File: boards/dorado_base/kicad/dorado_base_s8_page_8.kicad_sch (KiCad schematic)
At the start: 19 parts, among them j07 74LS251, j09 74LS251, k07 74LS174, k08 74LS174, k09 74LS174, k19 74LS138, k20 74LS85, k21a 74LS04, k21b 74LS04, k22 74LS151, k23a 74LS00

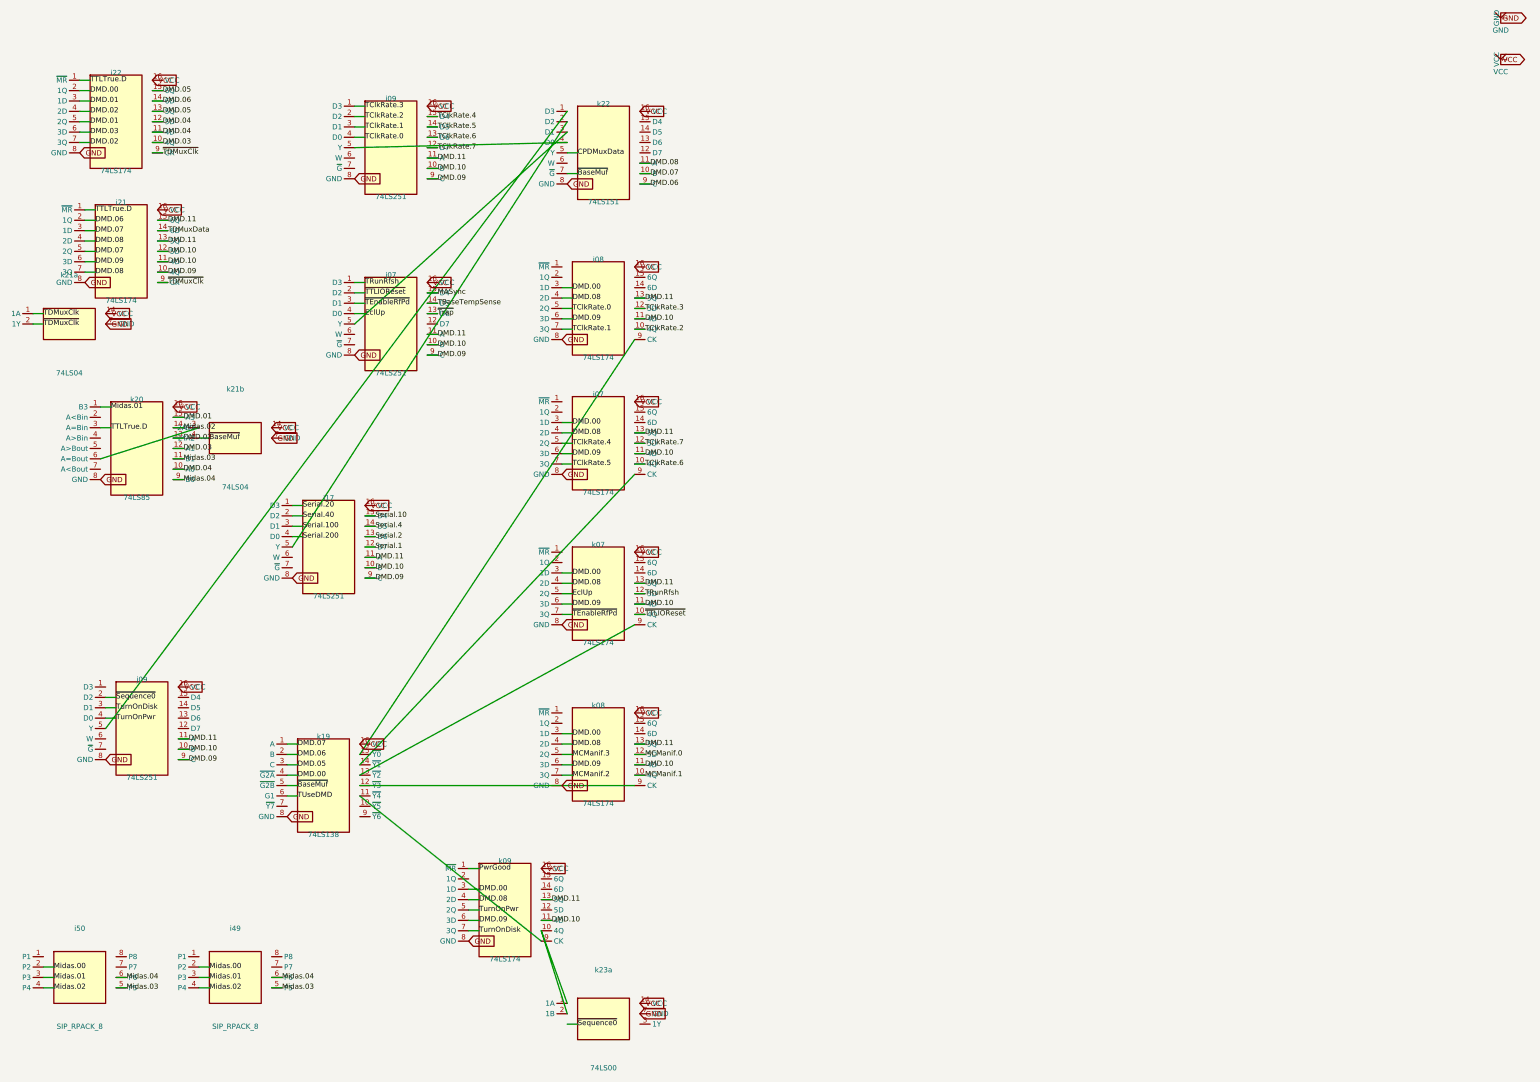
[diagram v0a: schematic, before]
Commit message: kicad export: faithful per-component symbols + path-aware wire routing
Switches the exporter from generic DIP symbols + straight-line pin-to-pin
wires to a per-component lib_symbol whose body matches the source bbox
and whose pins land at the placed pin_positions. The KiCad-rendered
schematic now reflects the original drawing's chip layout instead of an
auto-laid-out re-draw.

- synth_faithful_symbol(refdes, part, comp, scale): emits a unique
  user:_chip_<refdes> lib_symbol per component. Body shrunk by PIN_LENGTH
  on each side so pin lines extend visibly to the schematic dot. Pin
  (at) coords snapped to the 50-mil grid; angle picked from which body
  edge the pin is closest to.
- gen_sch chooses faithful when the component has pin_positions, else
  falls back to the existing generic synth_symbol path (so partly-
  transcribed sheets still export). pin_endpoint_mm in the faithful
  branch uses snapped local offsets so the absolute pin position equals
  instance_origin + offset, both grid-aligned (clears endpoint_off_grid).
- Wire emission: when net.path is set, emit one (wire) per consecutive
  polyline pair, snapped to grid. When absent, fall back to a one-corner
  Manhattan H-then-V route between each endpoint pair instead of a
  diagonal — gives KiCad something loadable until the tracer fills paths
  in. (Net path is consumed end-to-end through (wire (pts ...)).)
- Junctions: per-sheet sheets[].junctions emit (junction (at x y))
  blocks so KiCad's renderer draws connection dots where two wires
  cross AND connect.

Sheet 5 (full pin_positions, no split-gates) goes from
"blocking(35): endpoint_off_grid=11, power_pin_not_driven=24" to
PASS — only cross-sheet noise remains. Sheets 7 and 8 stay blocking=0
with their pre-existing pin_to_pin graph bugs unchanged.

Co-Authored-By: Claude Opus 4.7 (1M context) <noreply@anthropic.com>
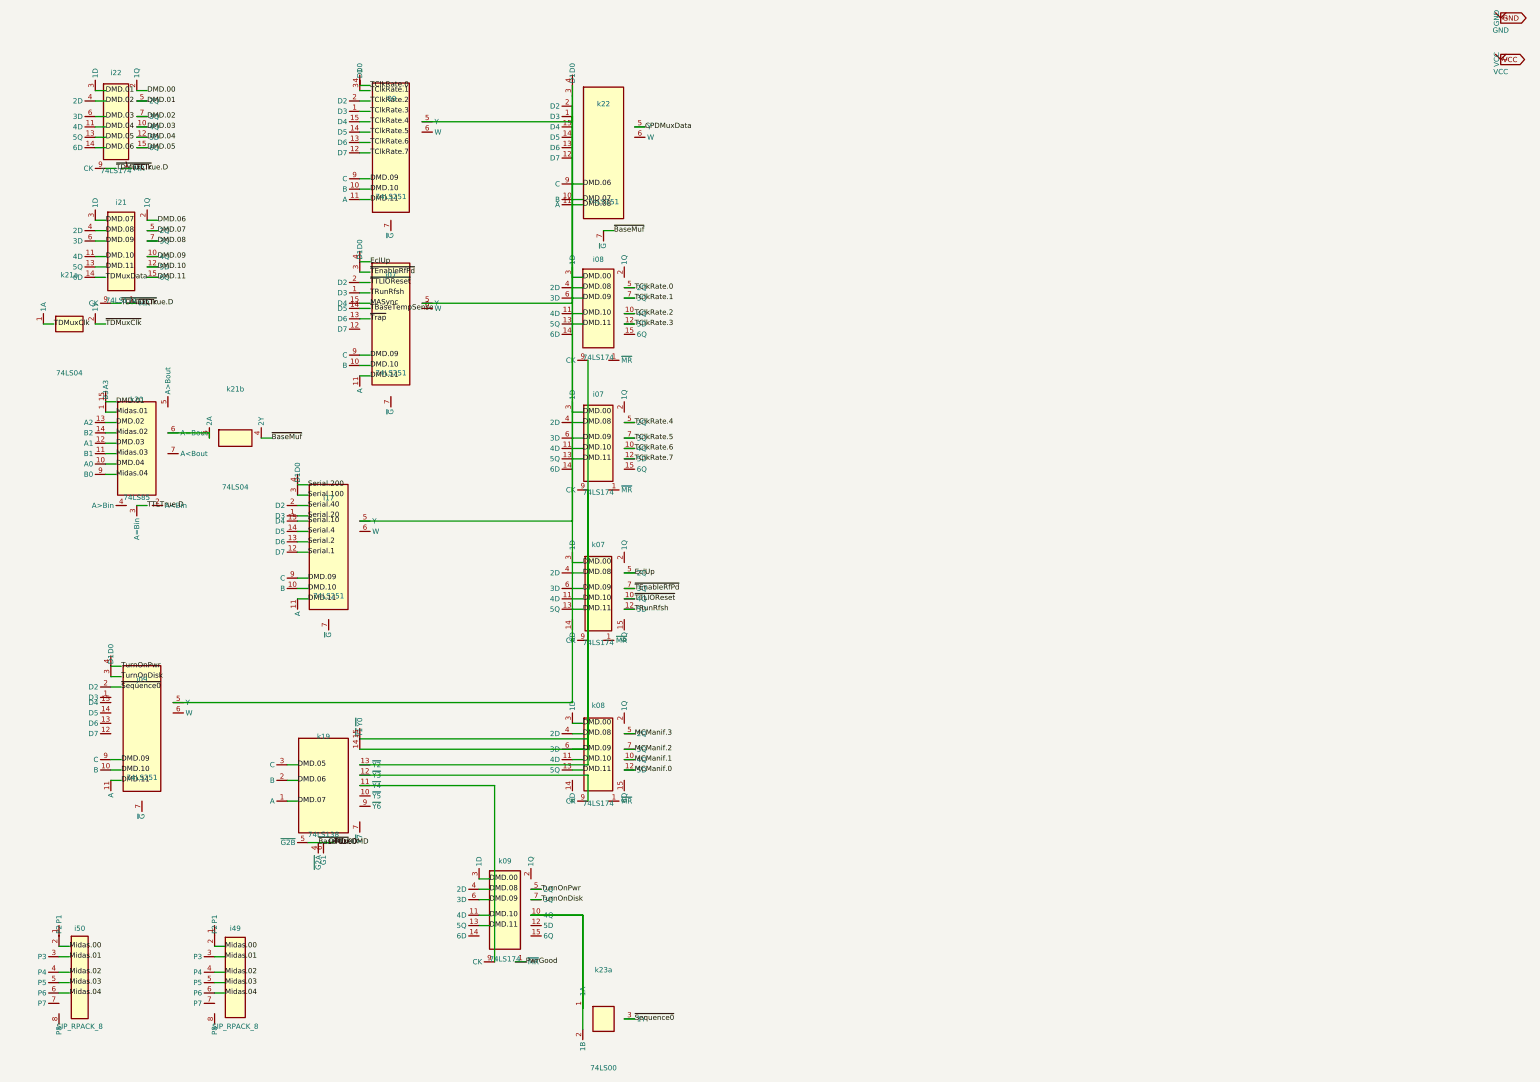
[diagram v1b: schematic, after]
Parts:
- i07: symbol user:74LS174 -> user:_chip_i07
- i08: symbol user:74LS174 -> user:_chip_i08
- i09: symbol user:74LS251 -> user:_chip_i09
- i17: symbol user:74LS251 -> user:_chip_i17
- i21: symbol user:74LS174 -> user:_chip_i21
- i22: symbol user:74LS174 -> user:_chip_i22
- i49: symbol user:SIP_RPACK_8 -> user:_chip_i49
- i50: symbol user:SIP_RPACK_8 -> user:_chip_i50
- j07: symbol user:74LS251 -> user:_chip_j07
- j09: symbol user:74LS251 -> user:_chip_j09
- k07: symbol user:74LS174 -> user:_chip_k07
- k08: symbol user:74LS174 -> user:_chip_k08
- k09: symbol user:74LS174 -> user:_chip_k09
- k19: symbol user:74LS138 -> user:_chip_k19
- k20: symbol user:74LS85 -> user:_chip_k20
- k21a: symbol user:74LS04_a -> user:_chip_k21a
- k21b: symbol user:74LS04_b -> user:_chip_k21b
- k22: symbol user:74LS151 -> user:_chip_k22
- k23a: symbol user:74LS00_a -> user:_chip_k23a
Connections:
- net TUseDMD is gone; now on net DMD.00: k19.6 (G1)
- net ~{BaseMuf} is gone; now on net DMD.00: k19.5 (~{G2B}), k21b.4 (2Y), k22.7 (~{G})
- net DMD.09: now also i07.9 (CK), i08.9 (CK), k07.9 (CK), k19.13 (~{Y2}), k19.14 (~{Y1}), k19.15 (~{Y0})
- net GND: no longer i07.8 (GND), i08.8 (GND), i09.8 (GND), i17.8 (GND), i21.8 (GND), i22.8 (GND), j07.8 (GND), j09.8 (GND), k07.8 (GND), k08.8 (GND), k08.9 (CK), k09.8 (GND), k19.12 (~{Y3}), k19.8 (GND), k20.8 (GND), k21a.7 (GND), k21b.7 (GND), k22.8 (GND), k23a.7 (GND)
- net VCC: no longer i07.16 (VCC), i08.16 (VCC), i09.16 (VCC), i17.16 (VCC), i21.16 (VCC), i22.16 (VCC), j07.16 (VCC), j09.16 (VCC), k07.16 (VCC), k08.16 (VCC), k09.16 (VCC), k19.16 (VCC), k20.16 (VCC), k21a.14 (VCC), k21b.14 (VCC), k22.16 (VCC), k23a.14 (VCC)
- net ~{Sequence0}: now also k23a.3 (1Y)
- net at i17.5 (Y), k22.2 (D2): now also i09.5 (Y), j07.5 (Y), j09.5 (Y), k22.1 (D3), k22.3 (D1), k22.4 (D0)
- new net: k08.9 (CK), k19.12 (~{Y3})
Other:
- moved on the sheet: i49, i50

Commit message: kicad export: fix pin-tip / polyline snap mismatch (1.27 mm off-grid)
Two code paths emitted absolute mm coords differently:

  pin tip   = _snap(M + cx_px*s) + _snap((ix-cx_px)*s)      # double-snap
  polyline  = _snap(M + p[0]*s)                              # single-snap

`_snap(a) + _snap(b) != _snap(a+b)` in general — the difference is 0 or
±1 grid unit. On Z80 SBC, a hand-traced wire from J1.2 to U1.14 had its
endpoint at the polyline's snapped coord (71.12, 76.20) while the pin
tip lived at the double-snapped coord (72.39, 74.93). KiCad reported
wire_dangling and 8 other short wires had the same workaround applied
(converted to label nets to dodge it).

Fix:
- synth_faithful_symbol now derives lib-symbol pin coords from the
  absolute pin tip (single-snap) minus the instance origin, instead of
  snapping the local offset directly. The local pin offset is no longer
  guaranteed to be a whole grid unit — body and pin can drift up to
  ~0.6 mm relative to each other — but the absolute pin tip is now
  always on grid AND agrees with every other coord-emitting path.
- gen_sch's faithful branch uses the same single-snap formula for
  pin_endpoint_mm.

This makes pin tips, polyline points, junctions, and discrete pins all
share one snap convention. Validated on Z80 SBC: RS232_TX (a workaround
label) converted back to wire + path produces wire_dangling=0.

Regression: dorado_base sheets 5/7/8, z80_sbc sheet 1, exidy_440 sheet 1
all stay blocking=0. Pre-existing graph wiring errors (pin_to_pin,
multiple_net_names) unchanged.

Removes bugs/polyline-pin-snap-mismatch.md.

Co-Authored-By: Claude Opus 4.7 (1M context) <noreply@anthropic.com>
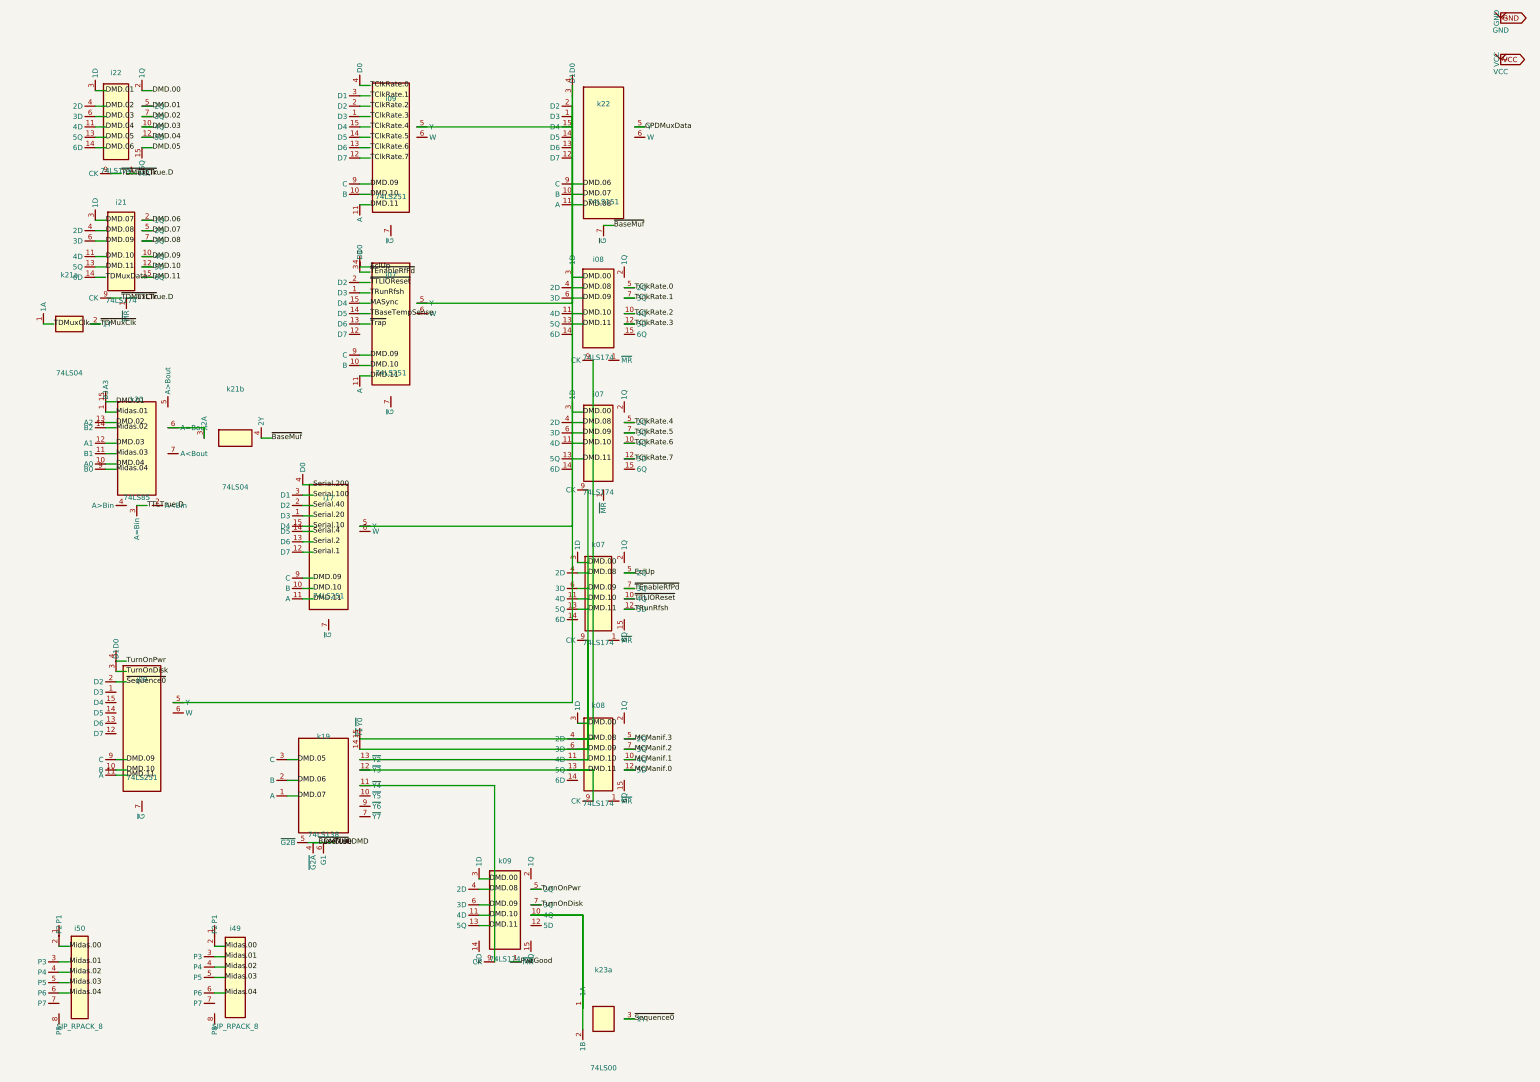
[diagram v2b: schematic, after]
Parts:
- i07, i08, i09, i17, i21, i22, j07, j09, k07, k08, k09, k19, k20, k22: footprint (none) -> Package_DIP:DIP-16_W7.62mm
- i49, i50: footprint (none) -> Package_DIP:DIP-8_W7.62mm
- k21a, k21b, k23a: footprint (none) -> Package_DIP:DIP-14_W7.62mm
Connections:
- net DMD.08 is gone; now on net DMD.00: i07.4 (2D), i08.4 (2D), i21.4 (2D), i21.7 (3Q), k07.4 (2D), k08.4 (2D), k09.4 (2D), k22.11 (A)
- net DMD.09 is gone; now on net DMD.00: i07.6 (3D), i07.9 (CK), i08.6 (3D), i08.9 (CK), i09.9 (C), i17.9 (C), i21.10 (4Q), i21.6 (3D), j07.9 (C), j09.9 (C), k07.6 (3D), k07.9 (CK), k08.6 (3D), k09.6 (3D), k19.13 (~{Y2}), k19.14 (~{Y1}), k19.15 (~{Y0})
- net DMD.10 is gone; now on net DMD.00: i07.11 (4D), i08.11 (4D), i09.10 (B), i17.10 (B), i21.11 (4D), i21.12 (5D), j07.10 (B), j09.10 (B), k07.11 (4D), k08.11 (4D), k09.11 (4D)
- net DMD.11 is gone; now on net DMD.00: i07.13 (5Q), i08.13 (5Q), i09.11 (A), i17.11 (A), i21.13 (5Q), i21.15 (6Q), j07.11 (A), j09.11 (A), k07.13 (5Q), k08.13 (5Q), k09.13 (5Q)
- net DMD.00: now also k08.9 (CK), k19.12 (~{Y3})
- net at i09.5 (Y), i17.5 (Y), j07.5 (Y)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: now also k22.15 (D4)
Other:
- moved on the sheet: i07, i09, i17, i21, i22, j07, j09, k07, k08, k21a, k21b, k22
